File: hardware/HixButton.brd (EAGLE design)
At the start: 54.6 x 20.1 mm, 29 parts, among them J1 FTDI, U1 ESP8266(ESP12E)V2, U2 TPS3839L30, U3 CN3058E, U4 WS2812

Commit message: routing complete
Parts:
- moved C1 8.89 mm to (40.6, 67.3), turned to 180 degrees
- moved R1 7.41 mm to (33.0, 71.1), turned to 180 degrees
- moved R10 4.02 mm to (33.0, 67.3), turned to 180 degrees
- moved R11 1.27 mm to (33.0, 63.5), turned to 180 degrees
- moved R12 1.27 mm to (40.6, 63.5), turned to 180 degrees
- moved R2 1.27 mm to (40.6, 71.1)
- turned C10 to 180 degrees
- turned L1 to 270 degrees
- turned L2 to 270 degrees
- turned R4 to 270 degrees
- turned STAYAWAKE to 0 degrees
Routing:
- net GND: track 0.00 -> 129.4 mm, vias 0 -> 3
- net 3.3V: track 0.00 -> 103.0 mm, vias 0 -> 1
- net RXD: track 0.00 -> 68.3 mm, vias 0 -> 1
- net N$5: track 0.00 -> 63.8 mm, vias 0 -> 2
- net TXD: track 0.00 -> 55.6 mm, vias 0 -> 1
- net N$3: track 0.00 -> 49.7 mm, vias 0 -> 1
- net RGB: track 0.00 -> 43.9 mm, vias 0 -> 3
- net N$4: track 0.00 -> 40.8 mm, vias 0 -> 2
- net N$12: track 0.00 -> 35.8 mm
- net N$13: track 0.00 -> 28.9 mm
- net 5.0V: track 0.00 -> 17.6 mm
- net N$9: track 0.00 -> 14.1 mm
- net N$2: track 0.00 -> 13.8 mm, vias 0 -> 1
- net N$6: track 0.00 -> 7.68 mm, vias 0 -> 2
- net N$11: track 0.00 -> 6.07 mm
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- added copper zone on layer 1, net 3.3V
- added copper zone on layer 16, net GND
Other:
- board size 54.6 x 20.1 mm -> 55.9 x 20.1 mm
- board text added: "+"
- board text added: "-"
- board text added: "HixButton v1.0.0 (C) HixField 2020"

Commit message: orderd pcbs
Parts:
- renumbered L1 to L1(GRN), L2 to L2(RED)
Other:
- board text added: "(C) 2020 HixField.com"
- board text added: "HixButton v1.0.0"
- board text removed: "HixButton v1.0.0 (C) HixField 2020"

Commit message: update readme
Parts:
- J1: value FTDI -> FTDIFTDI_ANGLED; device 0_HixField:FTDI -> 0_HixField:FTDI_ANGLED
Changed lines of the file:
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@@
 <grid distance="50" unitdist="mil" unit="mil" style="lines" multiple="1" display="no" altdistance="5" altunitdist="mil" altunit="mil"/>
 <layers>
-<layer number="1" name="Top" color="4" fill="1" visible="no" active="yes"/>
+<layer number="1" name="Top" color="4" fill="1" visible="yes" active="yes"/>
 <layer number="2" name="Route2" color="16" fill="1" visible="no" active="no"/>
 <layer number="3" name="Route3" color="17" fill="1" visible="no" active="no"/>
@@
 <layer number="16" name="Bottom" color="1" fill="1" visible="yes" active="yes"/>
 <layer number="17" name="Pads" color="2" fill="1" visible="yes" active="yes"/>
-<layer number="18" name="Vias" color="2" fill="1" visible="no" active="yes"/>
-<layer number="19" name="Unrouted" color="6" fill="1" visible="no" active="yes"/>
+<layer number="18" name="Vias" color="2" fill="1" visible="yes" active="yes"/>
+<layer number="19" name="Unrouted" color="6" fill="1" visible="yes" active="yes"/>
 <layer number="20" name="Dimension" color="24" fill="1" visible="yes" active="yes"/>
-<layer number="21" name="tPlace" color="7" fill="1" visible="no" active="yes"/>
-<layer number="22" name="bPlace" color="7" fill="1" visible="no" active="yes"/>
-<layer number="23" name="tOrigins" color="15" fill="1" visible="no" active="yes"/>
-<layer number="24" name="bOrigins" color="15" fill="1" visible="no" active="yes"/>
-<layer number="25" name="tNames" color="7" fill="1" visible="no" active="yes"/>
+<layer number="21" name="tPlace" color="7" fill="1" visible="yes" active="yes"/>
+<layer number="22" name="bPlace" color="7" fill="1" visible="yes" active="yes"/>
+<layer number="23" name="tOrigins" color="15" fill="1" visible="yes" active="yes"/>
+<layer number="24" name="bOrigins" color="15" fill="1" visible="yes" active="yes"/>
+<layer number="25" name="tNames" color="7" fill="1" visible="yes" active="yes"/>
 <layer number="26" name="bNames" color="7" fill="1" visible="yes" active="yes"/>
 <layer number="27" name="tValues" color="7" fill="1" visible="no" active="yes"/>
-<layer number="28" name="bValues" color="7" fill="1" visible="yes" active="yes"/>
+<layer number="28" name="bValues" color="7" fill="1" visible="no" active="yes"/>
 <layer number="29" name="tStop" color="7" fill="3" visible="no" active="yes"/>
 <layer number="30" name="bStop" color="7" fill="6" visible="no" active="yes"/>
@@
 <layer number="37" name="tTest" color="7" fill="1" visible="no" active="yes"/>
 <layer number="38" name="bTest" color="7" fill="1" visible="no" active="yes"/>
-<layer number="39" name="tKeepout" color="4" fill="11" visible="no" active="yes"/>
-<layer number="40" name="bKeepout" color="1" fill="11" visible="no" active="yes"/>
-<layer number="41" name="tRestrict" color="4" fill="10" visible="no" active="yes"/>
-<layer number="42" name="bRestrict" color="1" fill="10" visible="no" active="yes"/>
+<layer number="39" name="tKeepout" color="4" fill="11" visible="yes" active="yes"/>
+<layer number="40" name="bKeepout" color="1" fill="11" visible="yes" active="yes"/>
+<layer number="41" name="tRestrict" color="4" fill="10" visible="yes" active="yes"/>
+<layer number="42" name="bRestrict" color="1" fill="10" visible="yes" active="yes"/>
 <layer number="43" name="vRestrict" color="2" fill="10" visible="no" active="yes"/>
 <layer number="44" name="Drills" color="7" fill="1" visible="no" active="yes"/>
@@
 <layer number="49" name="Reference" color="7" fill="1" visible="no" active="yes"/>
 <layer number="50" name="dxf" color="7" fill="1" visible="no" active="no"/>
-<layer number="51" name="tDocu" color="7" fill="1" visible="no" active="yes"/>
+<layer number="51" name="tDocu" color="7" fill="1" visible="yes" active="yes"/>
 <layer number="52" name="bDocu" color="7" fill="1" visible="yes" active="yes"/>
 <layer number="53" name="tGND_GNDA" color="7" fill="9" visible="no" active="no"/>
@@
 </layers>
 <board>
+<fusionsync huburn="a.cGVyc29uYWw6dWUyZDExMjg2" projecturn="a.cGVyc29uYWw6dWUyZDExMjg2IzIwMjAxMjEyMzYxODc5OTUx" f3durn="urn:adsk.wipprod:dm.lineage:ODmNFmSTTw6yJyLLxPKMkg" pcbguid="68981e99-a15c-4b3f-9ce2-2bfe9745f1f3" lastpulledtime="" lastsyncedchangeguid="" latestrevisionid="05602d83-9cca-4a3b-8386-dc293eb8931c" lastsyncedrevisionid="05602d83-9cca-4a3b-8386-dc293eb8931c" lastboardhashguid="5be2f684-2e16-bcde-2481-cb733079b963" lastpushedtime="2020-12-12T02:13:22Z" linktopcb3d="true"/>
 <plain>
 <wire x1="28.194" y1="57.15" x2="84.054" y2="57.15" width="0" layer="20"/>
@@
 <attribute name="SPICEPREFIX" value="C" x="60.96" y="133.35" size="1.778" layer="27" rot="R180" display="off"/>
 </element>
-<element name="J1" library="0_HixField" library_urn="urn:adsk.eagle:library:13392178" package="FTDI" package3d_urn="urn:adsk.eagle:package:12836035/3" value="FTDI" x="81.28" y="63.5" smashed="yes">
+<element name="J1" library="0_HixField" library_urn="urn:adsk.eagle:library:13392178" package="FTDI_ANGLED" package3d_urn="urn:adsk.eagle:package:25353491/8" value="FTDIFTDI_ANGLED" x="81.28" y="63.5" smashed="yes">
 <attribute name="NAME" x="81.407" y="58.547" size="0.762" layer="25" rot="R180" align="center"/>
 </element>
@@
 </note>
 <note version="8.3" severity="warning">
+Since Version 8.3, EAGLE supports Fusion synchronisation.
+This feature will not be available in this version and saving
+the document will break the link to the Fusion PCB feature.
+</note>
+<note version="8.3" severity="warning">

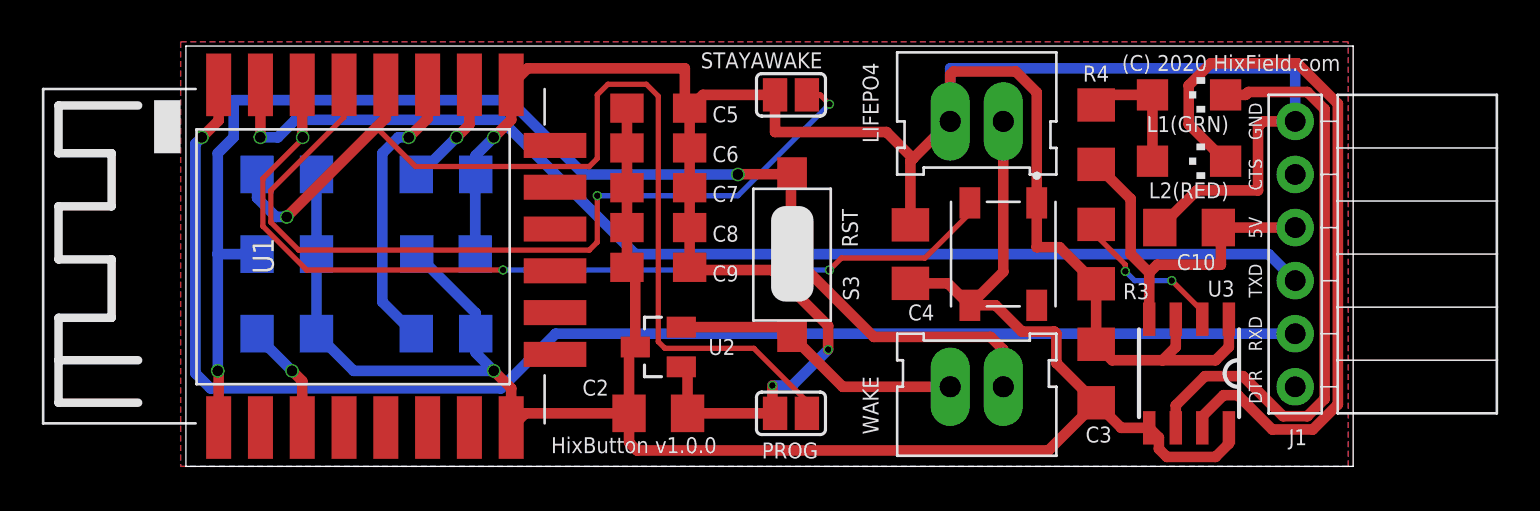
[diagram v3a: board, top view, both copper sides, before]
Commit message: v1.1.0 fix voltage supervisor
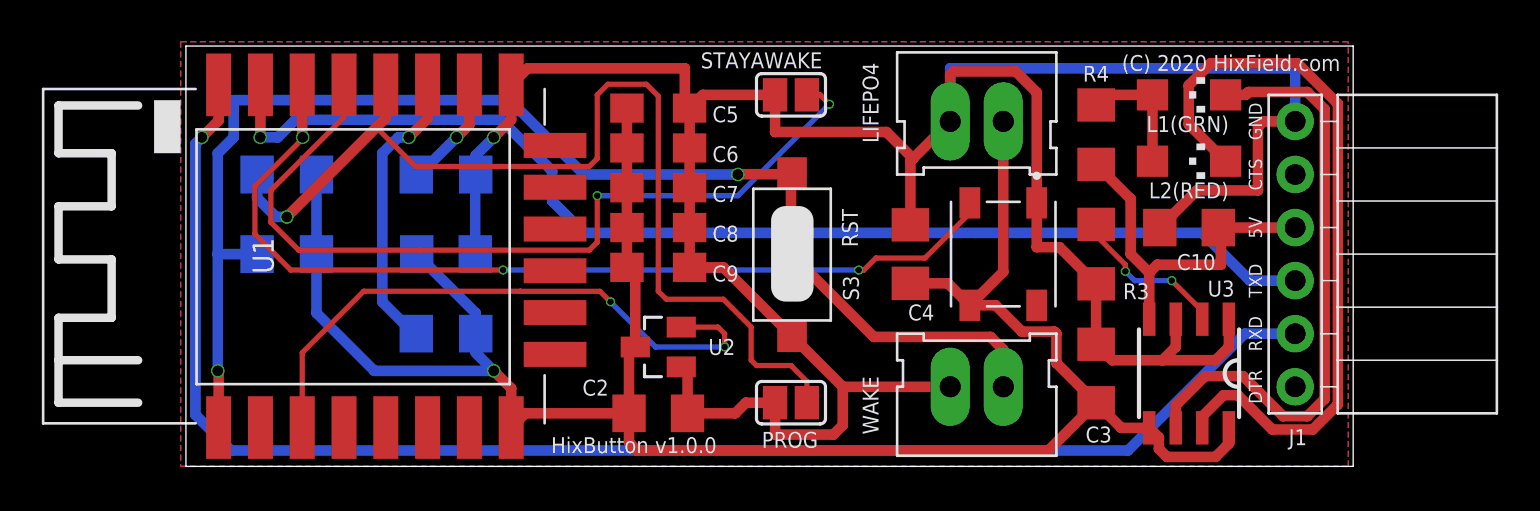
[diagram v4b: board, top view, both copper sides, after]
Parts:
- removed R11: 10K, rcl:R1206
- moved PROG 0.51 mm to (57.1, 60.2)
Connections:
- removed net N$8: R11.1, U1.ENABLE
- removed net N$9: S3.1, U2.2, WAKE.2
- new net N$7: U1.ENABLE, U2.2
- net 3.3V: no longer R11.2
- net GND: now also S3.1, WAKE.2
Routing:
- net N$7: track 0.00 -> 29.0 mm, vias 0 -> 2
- net N$9: track 14.1 -> 0.00 mm
- net GND: track 129.4 -> 137.6 mm, vias 3 -> 1
- net N$8: track 5.39 -> 0.00 mm, vias 1 -> 0
- net RXD: track 68.3 -> 71.9 mm
- net TXD: track 55.6 -> 56.4 mm
- net RGB: track 43.9 -> 44.6 mm
- net 3.3V: track 103.0 -> 102.4 mm

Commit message: v1.1.0 production
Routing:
- net N$12: track 35.8 -> 36.9 mm
- net N$13: track 28.9 -> 29.5 mm
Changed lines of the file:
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@@
 <class number="1" name="power" width="0.508" drill="0.254">
 </class>
-<class number="2" name="signal" width="0.254" drill="0">
+<class number="2" name="signal" width="0.254" drill="0.127">
 </class>
 </classes>
-<designrules name="jlcpcb-2layers *">
+<designrules name="jlcpcb-2layers_more_margen">
 <description language="en">&lt;b&gt;JLCPCB design rules (2 layers)&lt;/b&gt;
 &lt;ul&gt;
@@
 <attribute name="NAME" x="78.105" y="70.739" size="0.762" layer="25" rot="R180"/>
 <attribute name="POPULARITY" value="28" x="5.08" y="55.245" size="1.778" layer="27" rot="R270" display="off"/>
-<attribute name="VALUE" x="74.295" y="70.612" size="0.762" layer="27" rot="R90"/>
 </element>
 <element name="LIFEPO4" library="0_HixField" library_urn="urn:adsk.eagle:library:13392178" package="XH2P" package3d_urn="urn:adsk.eagle:package:12836045/3" value="XH2P" x="67.31" y="73.66" smashed="yes" rot="R90">
@@
 <wire x1="81.28" y1="76.2" x2="64.77" y2="76.2" width="0.508" layer="16"/>
 <wire x1="64.77" y1="76.2" x2="64.77" y2="73.66" width="0.508" layer="16"/>
-<polygon width="0.508" layer="16">
+<polygon width="0.508" layer="16" isolate="0.25">
 <vertex x="27.94" y="77.47"/>
 <vertex x="27.94" y="57.15"/>
@@
 <wire x1="78.105" y1="58.239" x2="78.105" y2="58.995" width="0.508" layer="1"/>
 <wire x1="75.13758125" y1="57.604" x2="77.47" y2="57.604" width="0.508" layer="1"/>
-<polygon width="0.508" layer="1">
+<polygon width="0.508" layer="1" isolate="0.25">
 <vertex x="27.94" y="77.47"/>
 <vertex x="27.94" y="57.15"/>
@@
 <contactref element="U3" pad="7"/>
 <wire x1="77.24358125" y1="76.442" x2="76.184" y2="75.38241875" width="0.508" layer="1"/>
-<wire x1="80.17975" y1="58.917" x2="82.12625" y2="58.917" width="0.508" layer="1"/>
-<wire x1="82.12625" y1="58.917" x2="83.323" y2="60.11375" width="0.508" layer="1"/>
-<wire x1="83.323" y1="60.11375" x2="83.323" y2="74.50625" width="0.508" layer="1"/>
+<wire x1="80.43375" y1="58.663" x2="82.50725" y2="58.663" width="0.508" layer="1"/>
+<wire x1="82.50725" y1="58.663" x2="83.577" y2="59.73275" width="0.508" layer="1"/>
+<wire x1="83.577" y1="59.73275" x2="83.577" y2="74.88725" width="0.508" layer="1"/>
 <wire x1="76.835" y1="58.995" x2="76.835" y2="59.54341875" width="0.508" layer="1"/>
 <wire x1="76.835" y1="59.54341875" x2="77.84858125" y2="60.557" width="0.508" layer="1"/>
 <wire x1="77.84858125" y1="60.557" x2="78.53975" y2="60.557" width="0.508" layer="1"/>
-<wire x1="78.53975" y1="60.557" x2="80.17975" y2="58.917" width="0.508" layer="1"/>
-<wire x1="83.323" y1="74.50625" x2="81.38725" y2="76.442" width="0.508" layer="1"/>
-<wire x1="81.38725" y1="76.442" x2="77.24358125" y2="76.442" width="0.508" layer="1"/>
+<wire x1="78.53975" y1="60.557" x2="80.43375" y2="58.663" width="0.508" layer="1"/>
+<wire x1="83.577" y1="74.88725" x2="82.02225" y2="76.442" width="0.508" layer="1"/>
+<wire x1="82.02225" y1="76.442" x2="77.24358125" y2="76.442" width="0.508" layer="1"/>
 <wire x1="76.184" y1="75.38241875" x2="76.184" y2="73.521" width="0.508" layer="1"/>
 <wire x1="76.184" y1="73.521" x2="77.95" y2="71.755" width="0.508" layer="1"/>
@@
 <contactref element="L1(GRN)" pad="C"/>
 <contactref element="U3" pad="6"/>
-<wire x1="82.688" y1="60.37678125" x2="81.86321875" y2="59.552" width="0.508" layer="1"/>
-<wire x1="82.688" y1="74.24321875" x2="81.86321875" y2="75.068" width="0.508" layer="1"/>
-<wire x1="82.688" y1="60.37678125" x2="82.688" y2="74.24321875" width="0.508" layer="1"/>
-<wire x1="81.86321875" y1="75.068" x2="79.04458125" y2="75.068" width="0.508" layer="1"/>
-<wire x1="79.04458125" y1="75.068" x2="78.90658125" y2="74.93" width="0.508" layer="1"/>
+<wire x1="82.815" y1="60.37678125" x2="81.86321875" y2="59.425" width="0.508" layer="1"/>
+<wire x1="82.815" y1="74.49721875" x2="82.11721875" y2="75.195" width="0.508" layer="1"/>
+<wire x1="82.815" y1="60.37678125" x2="82.815" y2="74.49721875" width="0.508" layer="1"/>
+<wire x1="82.11721875" y1="75.195" x2="79.17158125" y2="75.195" width="0.508" layer="1"/>
+<wire x1="79.17158125" y1="75.195" x2="78.90658125" y2="74.93" width="0.508" layer="1"/>
 <wire x1="78.90658125" y1="74.93" x2="77.95" y2="74.93" width="0.508" layer="1"/>
-<wire x1="80.69678125" y1="59.552" x2="81.86321875" y2="59.552" width="0.508" layer="1"/>
+<wire x1="80.82378125" y1="59.425" x2="81.86321875" y2="59.425" width="0.508" layer="1"/>
 <wire x1="76.962" y1="61.468" x2="75.565" y2="60.071" width="0.508" layer="1"/>
 <wire x1="76.962" y1="61.468" x2="78.78078125" y2="61.468" width="0.508" layer="1"/>
-<wire x1="78.78078125" y1="61.468" x2="80.69678125" y2="59.552" width="0.508" layer="1"/>
+<wire x1="78.78078125" y1="61.468" x2="80.82378125" y2="59.425" width="0.508" layer="1"/>
 <wire x1="75.565" y1="60.071" x2="75.565" y2="58.995" width="0.508" layer="1"/>
 </signal>
